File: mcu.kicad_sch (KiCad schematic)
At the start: 27 parts, among them J1 Conn_01x05, J4 USB_B_Micro, U1 STM32G473CCUx, Y1 8 MHz

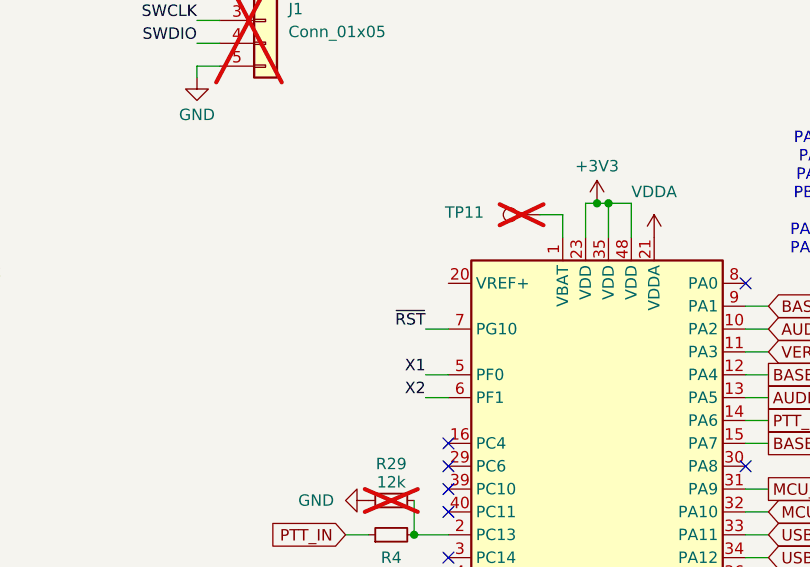
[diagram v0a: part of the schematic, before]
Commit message: VREF+ connected to VDDA
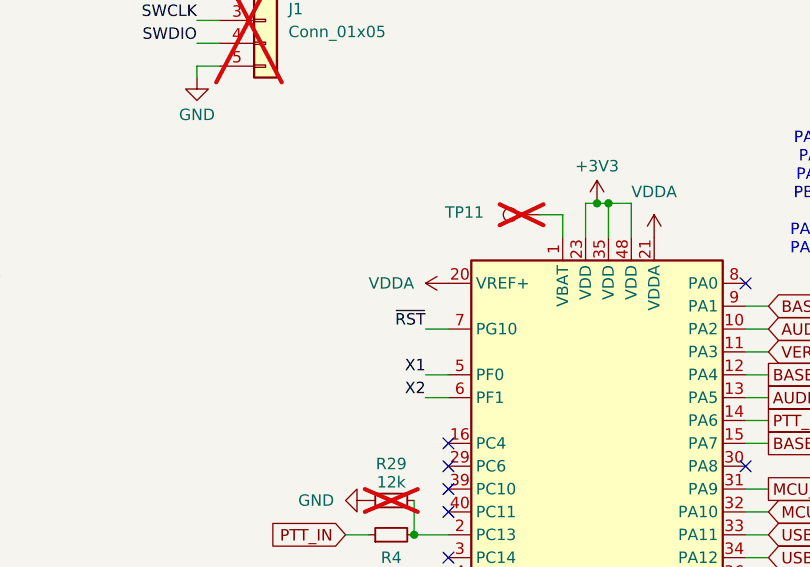
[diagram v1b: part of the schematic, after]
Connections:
- net VDDA: now also U1.20 (VREF+)
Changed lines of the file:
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@@
 	(title_block
 		(title "Micro17 - OpenRTX on a Module for ICOM radios")
-		(date "2024-04-04")
-		(rev "A")
+		(date "2024-09-10")
+		(rev "B")
 		(company "Wojciech SP5WWP, Mano ON6RF, Mutlu TA1MD et al.")
 		(comment 1 "M17 Project, OpenRTX")
@@
 					(unit 1)
 				)
+			)
+		)
+	)
+	(symbol
+		(lib_id "power:VDDA")
+		(at 121.92 66.04 90)
+		(unit 1)
+		(exclude_from_sim no)
+		(in_bom yes)
+		(on_board yes)
+		(dnp no)
+		(fields_autoplaced yes)
+		(property "Reference" "#PWR027"
+			(at 125.73 66.04 0)
+			(effects
+				(font
+					(size 1.27 1.27)
+				)
+				(hide yes)
+			)
+		)
+		(property "Value" "VDDA"
+			(at 118.11 66.0399 90)
+			(effects
+				(font
+					(size 1.27 1.27)
+				)
+				(justify left)
+			)
+		)
+		(property "Footprint" ""
+			(at 121.92 66.04 0)
+			(effects
+				(font
+					(size 1.27 1.27)
+				)
+				(hide yes)
+			)
+		)
+		(property "Datasheet" ""
+			(at 121.92 66.04 0)
+			(effects
+				(font
+					(size 1.27 1.27)
+				)
+				(hide yes)
+			)
+		)
+		(property "Description" "Power symbol creates a global label with name \"VDDA\""
+			(at 121.92 66.04 0)
+			(effects
+				(font
+					(size 1.27 1.27)
+				)
+				(hide yes)
+			)
+		)
+		(pin "1"
+		)
+		(instances
+			(project "micro17"
+				(path "/8b0d7f56-1962-40c9-8b95-6d4fe558acbc/9f9e0b5b-f07d-4ebd-b315-be375c62719d"
+					(reference "#PWR027")
+					(unit 1)
+				)
